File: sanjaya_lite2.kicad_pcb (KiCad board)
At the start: 2 copper layers, 73.5 x 77.5 mm, 112 parts, among them J1 12V_Out, J10 Adap_In, J11 DCDC_Bypass, J12 Conn_RS485, J13 Bat_Bypass+, J14 J_Bat, J15 Conn_420_1, J16 Conn_420_2, J17 Conn_420_3, J18 Conn_420_4, J19 Volt_check_5V, J2 J_SW_Esp, J20 Pwr_SW, J21 J_SW_Sim800, J22 UART_Sim800, J23 Bat_Prot_Bypass, J3 5V_Out, J4 J_LED, J5 VBat_Out, J6 Conn_I2C, J7 Conn_SPI, J8 Conn_I2C, J9 J_UART_DBG, Q1 PMOS_SI2369DS, Q2 BSS138, Q3 BSS138, SW1 SW_Reset, SW2 SW_Boot, U1 ESP32-WROOM-32, U2 MCP1700-3302E_SOT23, U3 SN65HVD75DR, U5 MCP3428

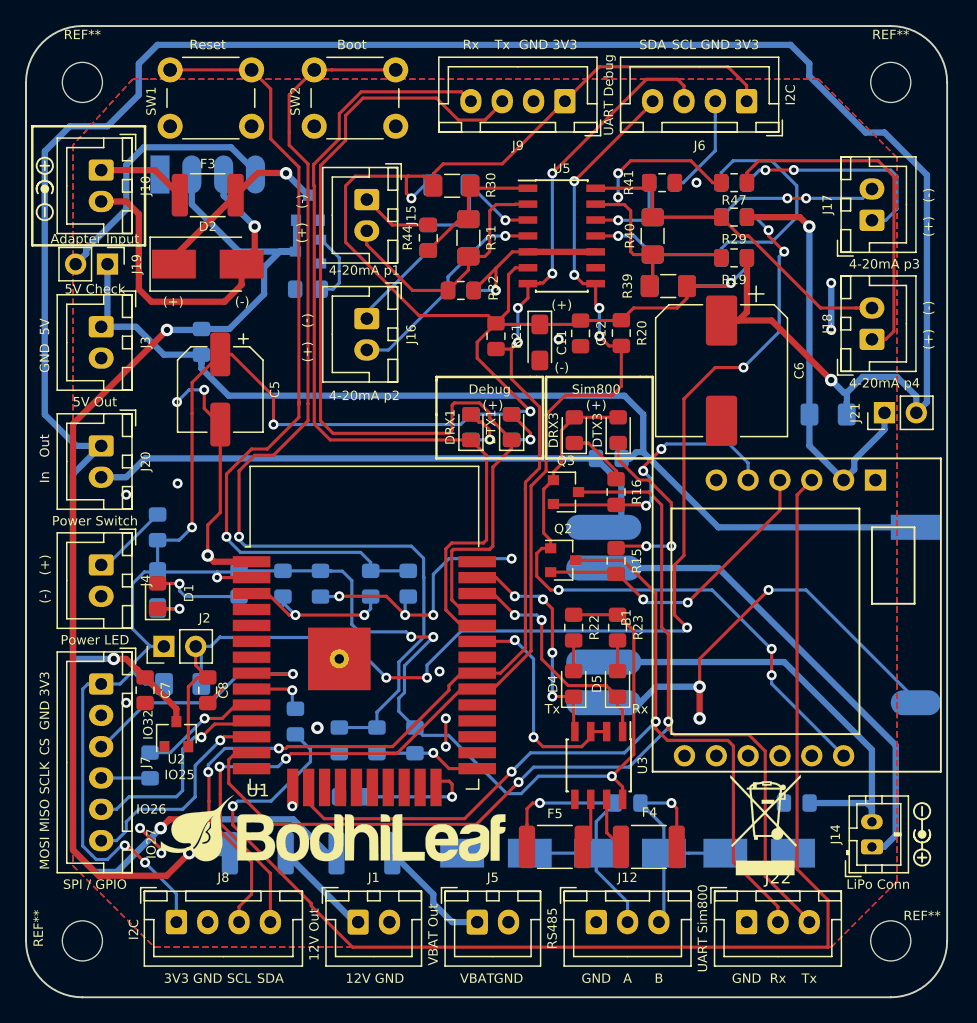
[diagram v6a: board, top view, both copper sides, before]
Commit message: Battery JST pin connections swapped. Copper pour restricted near Sim800 antenna area
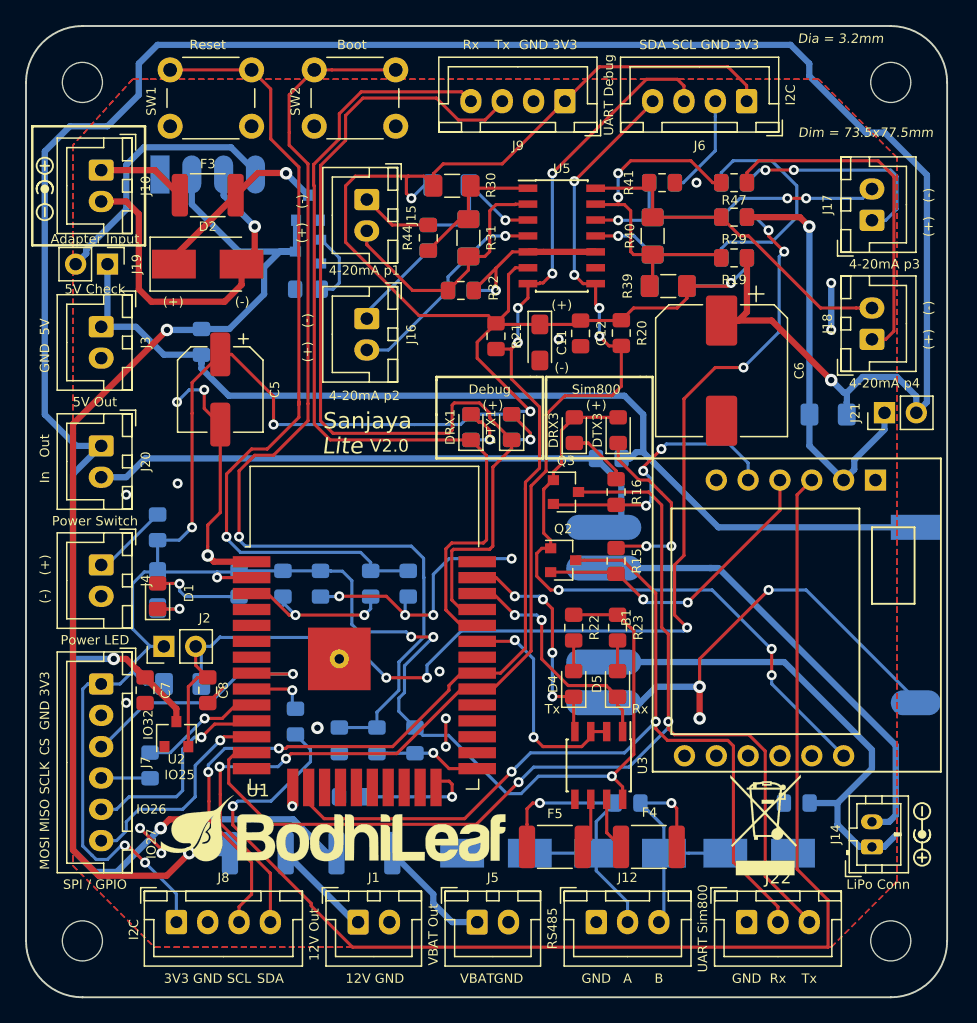
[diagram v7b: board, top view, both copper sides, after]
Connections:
- J14 pad 1: Net-(B3-Pad5) -> Net-(B3-Pad4)
- J14 pad 2: Net-(B3-Pad4) -> Net-(B3-Pad5)
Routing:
- net Net-(B3-Pad4): track 34.9 -> 38.0 mm
- net Net-(B3-Pad5): track 37.5 -> 35.7 mm
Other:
- board text added: "Dia = 3.2mm"
- board text added: "Dim = 73.5x77.5mm"
- board text added: "Lite"
- board text added: "Sanjaya"
- board text added: "V2.0"
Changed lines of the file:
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@@
   (general
     (thickness 1.6)
-    (drawings 133)
-    (tracks 998)
+    (drawings 138)
+    (tracks 1002)
     (zones 0)
     (modules 112)
@@
   (page A4)
   (layers
-    (0 F.Cu signal hide)
-    (31 B.Cu signal)
+    (0 F.Cu signal)
+    (31 B.Cu signal hide)
     (32 B.Adhes user hide)
-    (33 F.Adhes user hide)
+    (33 F.Adhes user)
     (34 B.Paste user hide)
-    (35 F.Paste user hide)
+    (35 F.Paste user)
     (36 B.SilkS user)
-    (37 F.SilkS user hide)
+    (37 F.SilkS user)
     (38 B.Mask user hide)
-    (39 F.Mask user hide)
+    (39 F.Mask user)
     (40 Dwgs.User user)
-    (41 Cmts.User user)
+    (41 Cmts.User user hide)
     (42 Eco1.User user hide)
     (43 Eco2.User user hide)
     (44 Edge.Cuts user)
     (45 Margin user)
-    (46 B.CrtYd user)
-    (47 F.CrtYd user hide)
-    (48 B.Fab user)
-    (49 F.Fab user hide)
+    (46 B.CrtYd user hide)
+    (47 F.CrtYd user)
+    (48 B.Fab user hide)
+    (49 F.Fab user)
   )
   (setup
@@
     (tags "mounting hole 3.2mm no annular m3 din965")
     (attr virtual)
-    (fp_text reference REF** (at 0 -3.8) (layer F.SilkS)
+    (fp_text reference REF** (at 0 -3.8) (layer F.SilkS) hide
       (effects (font (size 0.75 0.75) (thickness 0.1)))
     )
@@
     (tags "mounting hole 3.2mm no annular m3 din965")
     (attr virtual)
-    (fp_text reference REF** (at 0 -3.8) (layer F.SilkS)
+    (fp_text reference REF** (at 0 -3.8) (layer F.SilkS) hide
       (effects (font (size 0.75 0.75) (thickness 0.1)))
     )
@@
     (tags "mounting hole 3.2mm no annular m3 din965")
     (attr virtual)
-    (fp_text reference REF** (at 2.5 -2) (layer F.SilkS)
+    (fp_text reference REF** (at 2.5 -2) (layer F.SilkS) hide
       (effects (font (size 0.75 0.75) (thickness 0.1)))
     )
@@
     (tags "mounting hole 3.2mm no annular m3 din965")
     (attr virtual)
-    (fp_text reference REF** (at -3.5 -1 90) (layer F.SilkS)
+    (fp_text reference REF** (at -3.5 -1 90) (layer F.SilkS) hide
       (effects (font (size 0.75 0.75) (thickness 0.1)))
     )
@@
     )
     (pad 1 thru_hole roundrect (at 0 0 90) (size 1.2 1.75) (drill 0.75) (layers *.Cu *.Mask) (roundrect_rratio 0.208333)
-      (net 11 "Net-(B3-Pad5)"))
-    (pad 2 thru_hole oval (at 2 0 90) (size 1.2 1.75) (drill 0.75) (layers *.Cu *.Mask)
       (net 10 "Net-(B3-Pad4)"))
+    (pad 2 thru_hole oval (at 2 0 90) (size 1.2 1.75) (drill 0.75) (layers *.Cu *.Mask)
+      (net 11 "Net-(B3-Pad5)"))
     (model ${KISYS3DMOD}/Connector_JST.3dshapes/JST_PH_B2B-PH-K_1x02_P2.00mm_Vertical.wrl
       (at (xyz 0 0 0))
@@
       (xy 2.281939 1.776157) (xy 2.394294 1.868669) (xy 2.278086 1.706699)) (layer B.SilkS) (width 0.01))
   )
+  (gr_text "Dia = 3.2mm" (at 150.5 56.5) (layer F.SilkS)
+    (effects (font (size 0.75 0.75) (thickness 0.1) italic))
+  )
+  (gr_text "Dim = 73.5x77.5mm" (at 152.5 64) (layer F.SilkS)
+    (effects (font (size 0.75 0.75) (thickness 0.1) italic))
+  )
+  (gr_text V2.0 (at 114.5 89) (layer F.SilkS)
+    (effects (font (size 1 1) (thickness 0.15)))
+  )
+  (gr_text Lite (at 110.75 89) (layer F.SilkS)
+    (effects (font (size 1.3 1.3) (thickness 0.1) italic))
+  )
+  (gr_text Sanjaya (at 112.75 87) (layer F.SilkS)
+    (effects (font (size 1.3 1.3) (thickness 0.2)))
+  )
   (gr_text IO32 (at 95.25 111.25 90) (layer F.SilkS)
     (effects (font (size 0.75 0.75) (thickness 0.1)))
@@
   (segment (start 133.7 90) (end 134.2 89.5) (width 0.5) (layer B.Cu) (net 9))
   (segment (start 133.025 90) (end 133.7 90) (width 0.5) (layer B.Cu) (net 9))
+  (segment (start 150.25 117.5) (end 148.025 117.5) (width 0.5) (layer B.Cu) (net 10))
+  (segment (start 153 114.75) (end 150.25 117.5) (width 0.5) (layer B.Cu) (net 10))
   (segment (start 133 106.25) (end 146 106.25) (width 0.5) (layer B.Cu) (net 10))
-  (segment (start 153 113.25) (end 153 119) (width 0.5) (layer B.Cu) (net 10))
+  (segment (start 153 113.25) (end 153 114.75) (width 0.5) (layer B.Cu) (net 10))
   (segment (start 146 106.25) (end 153 113.25) (width 0.5) (layer B.Cu) (net 10))
-  (segment (start 153 117.9) (end 153 119) (width 0.5) (layer B.Cu) (net 10))
-  (segment (start 152.6 117.5) (end 153 117.9) (width 0.5) (layer B.Cu) (net 10))
-  (segment (start 148.025 117.5) (end 152.6 117.5) (width 0.5) (layer B.Cu) (net 10))
+  (segment (start 150.25 119.225) (end 150.25 117.5) (width 0.5) (layer B.Cu) (net 10))
+  (segment (start 152.025 121) (end 150.25 119.225) (width 0.5) (layer B.Cu) (net 10))
+  (segment (start 153 121) (end 152.025 121) (width 0.5) (layer B.Cu) (net 10))
+  (segment (start 153.975 121) (end 153 121) (width 0.5) (layer B.Cu) (net 10) (status 1000000))
+  (segment (start 154.9 120.075) (end 153.975 121) (width 0.5) (layer B.Cu) (net 10) (status 1000000))
   (segment (start 140 98.75) (end 140.25 98.75) (width 0.5) (layer B.Cu) (net 11))
   (segment (start 133 98.75) (end 140 98.75) (width 0.5) (layer B.Cu) (net 11))
-  (segment (start 153.975 121) (end 153 121) (width 0.5) (layer B.Cu) (net 11))
-  (segment (start 154.9 120.075) (end 153.975 121) (width 0.5) (layer B.Cu) (net 11))
-  (segment (start 154.9 112.9) (end 154.9 120.075) (width 0.5) (layer B.Cu) (net 11))
+  (segment (start 154.9 118.475) (end 154.375 119) (width 0.5) (layer B.Cu) (net 11))
+  (segment (start 154.375 119) (end 153 119) (width 0.5) (layer B.Cu) (net 11))
+  (segment (start 154.9 112.9) (end 154.9 118.475) (width 0.5) (layer B.Cu) (net 11))
   (segment (start 140.75 98.75) (end 154.9 112.9) (width 0.5) (layer B.Cu) (net 11))
   (segment (start 140 98.75) (end 140.75 98.75) (width 0.5) (layer B.Cu) (net 11))
@@
       )
     )
+  )
+  (zone (net 0) (net_name "") (layers F&B.Cu) (hatch edge 0.508)
+    (connect_pads (clearance 0.508))
+    (min_thickness 0.254)
+    (keepout (tracks allowed) (vias allowed) (copperpour not_allowed))
+    (fill (arc_segments 16) (thermal_gap 0.508) (thermal_bridge_width 0.508))
+    (polygon
+      (pts
+        (xy 151.75 90) (xy 158.75 90) (xy 158.75 100.25) (xy 158.75 101.75) (xy 158.75 115)
+        (xy 151.75 115)
+      )
+    )

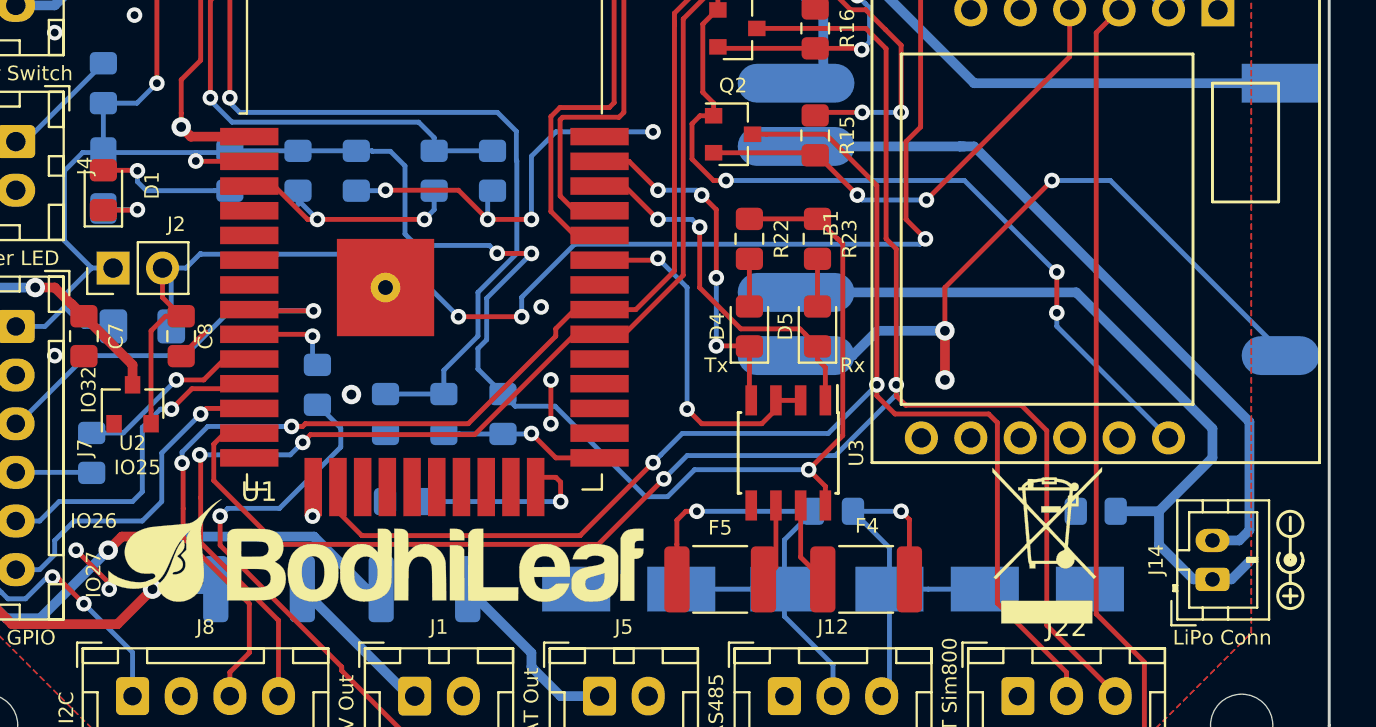
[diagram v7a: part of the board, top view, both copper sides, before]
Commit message: Reversed the battery polarity silk screen symbol as it was wrong. Added polarity indication on F.Silk for D1
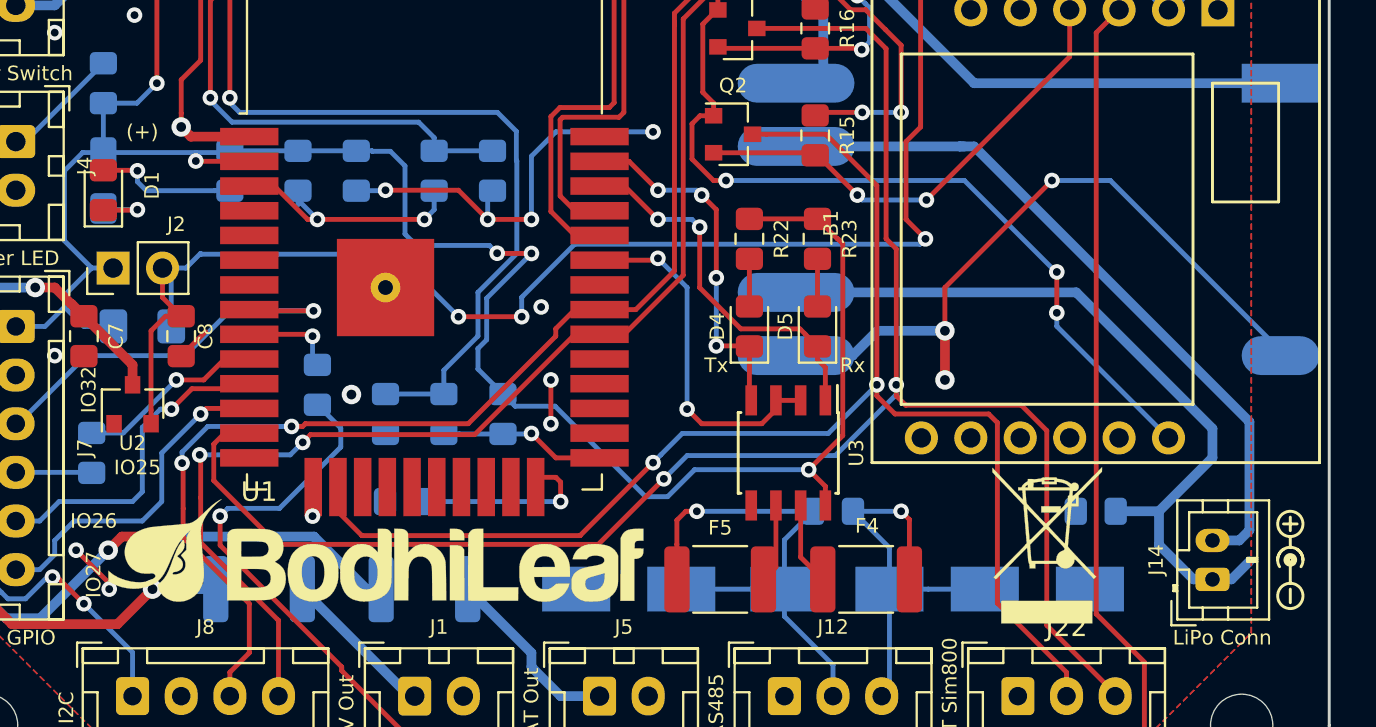
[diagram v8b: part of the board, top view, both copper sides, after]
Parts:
- turned G*** to 270 degrees
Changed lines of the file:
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@@
   (general
     (thickness 1.6)
-    (drawings 138)
+    (drawings 139)
     (tracks 1002)
     (zones 0)
@@
   )
   (module "Custom Silkscreens:Logo_silk_polarity_external_5x1.4mm" (layer F.Cu)
-    (at 157 120 90)
+    (at 157 120 270)
     (descr "Polarity logo, negative center, 5x1.4mm")
-    (fp_text reference G*** (at -0.9 0.6 90) (layer F.SilkS) hide
+    (fp_text reference G*** (at -0.9 0.6 270) (layer F.SilkS) hide
       (effects (font (size 0.0889 0.0889) (thickness 0.01778)))
     )
-    (fp_text value LOGO (at 1 0.6 90) (layer F.SilkS) hide
+    (fp_text value LOGO (at 1 0.6 270) (layer F.SilkS) hide
       (effects (font (size 0.0889 0.0889) (thickness 0.01778)))
     )
@@
       (xy 2.281939 1.776157) (xy 2.394294 1.868669) (xy 2.278086 1.706699)) (layer B.SilkS) (width 0.01))
   )
+  (gr_text "(+)" (at 98 98) (layer F.SilkS)
+    (effects (font (size 0.75 0.75) (thickness 0.1)))
+  )
   (gr_text "Dia = 3.2mm" (at 150.5 56.5) (layer F.SilkS)
